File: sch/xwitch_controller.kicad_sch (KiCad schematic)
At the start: 5 parts

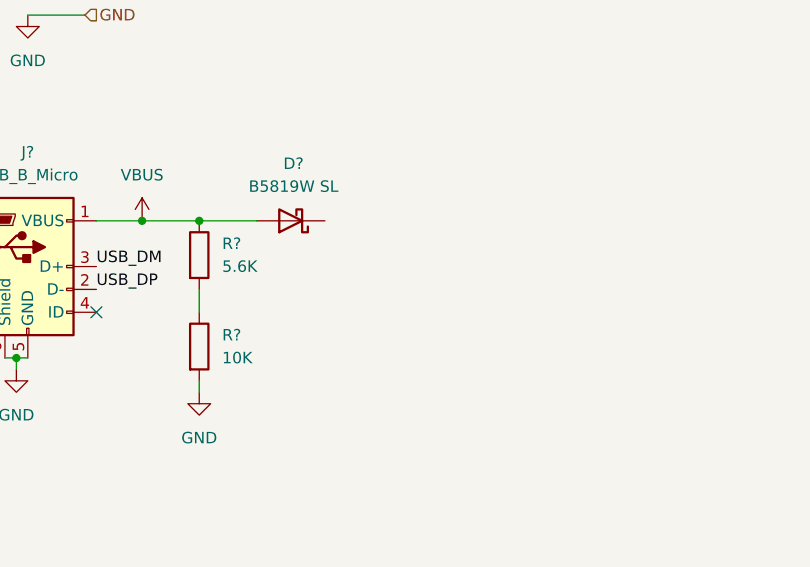
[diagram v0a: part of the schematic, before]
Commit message: added dc dc step down for rpi2040
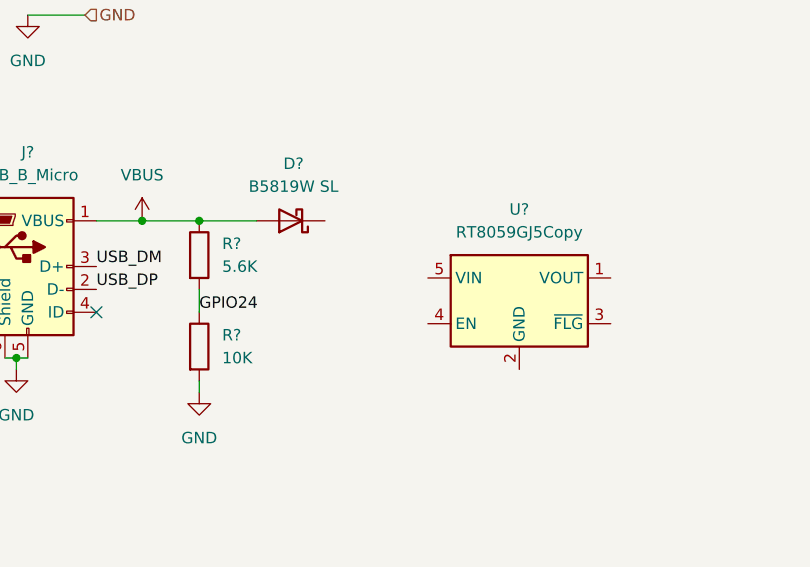
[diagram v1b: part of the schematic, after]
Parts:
- added U?: RT8059GJ5Copy, Package_TO_SOT_SMD:TSOT-23-5, symbol Power_Management:RT9742AGJ5F
- D?: LCSC C8598Copy -> C8598
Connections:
- net GPIO24: now reaches R?.1, R?.2
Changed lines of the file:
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@@
+    (effects (font (size 1.27 1.27)) (justify left bottom))
+  )
+  (label "GPIO24" (at 43.18 58.42 0)
     (effects (font (size 1.27 1.27)) (justify left bottom))
   )
@@
     )
     (pin "1")
+  )
+  (symbol (lib_id "Power_Management:RT9742AGJ5F") (at 78.74 57.15 0) (unit 1)
+    (in_bom yes) (on_board yes) (fields_autoplaced)
+    (property "Reference" "U?" (id 0) (at 78.74 46.99 0))
+    (property "Value" "RT8059GJ5Copy" (id 1) (at 78.74 49.53 0))
+    (property "Footprint" "Package_TO_SOT_SMD:TSOT-23-5" (id 2) (at 78.74 69.85 0)
+      (effects (font (size 1.27 1.27)) hide)
+    )
+    (property "Datasheet" "https://datasheet.lcsc.com/lcsc/1811100910_Richtek-Tech-RT8059GJ5_C20542.pdf" (id 3) (at 78.74 72.39 0)
+      (effects (font (size 1.27 1.27)) hide)
+    )
+    (property "LCSC" "C20542" (id 4) (at 78.74 57.15 0)
+      (effects (font (size 1.27 1.27)) hide)
+    )
+    (pin "1")
+    (pin "2")
+    (pin "3")
+    (pin "4")
+    (pin "5")
   )
   (symbol (lib_id "Connector:USB_B_Micro") (at 24.13 53.34 0) (unit 1)
@@
       (effects (font (size 1.27 1.27)) hide)
     )
-    (property "LCSC" "C8598Copy" (id 4) (at 53.34 48.26 0)
+    (property "LCSC" "C8598" (id 4) (at 53.34 48.26 0)
       (effects (font (size 1.27 1.27)) hide)
     )

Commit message: update pico schematics
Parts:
- removed U?: RT8059GJ5Copy, Package_TO_SOT_SMD:TSOT-23-5, symbol Power_Management:RT9742AGJ5F
- added C? (x2): 47u, Capacitor_SMD:C_0805_2012Metric_Pad1.18x1.45mm_HandSolder, symbol Device:C
- added C?: 2.2u, Inductor_SMD:L_0402_1005Metric_Pad0.77x0.64mm_HandSolder, symbol Device:C
- added C?: 100n, Inductor_SMD:L_0402_1005Metric_Pad0.77x0.64mm_HandSolder, symbol Device:C
- added L?: 2u2, Inductor_SMD:L_0603_1608Metric_Pad1.05x0.95mm_HandSolder, symbol Device:L
- added R?: 604K, Inductor_SMD:L_0402_1005Metric_Pad0.77x0.64mm_HandSolder, symbol Device:R
- added R?: 137K, Inductor_SMD:L_0402_1005Metric_Pad0.77x0.64mm_HandSolder, symbol Device:R
- added R? (x2): 1K, Inductor_SMD:L_0402_1005Metric_Pad0.77x0.64mm_HandSolder, symbol Device:R
- added SW?: C2689642, usb_xwitch:SW_SPST_CK_PTS636_SP43_SMTR, symbol Switch:SW_SPST
- added U?: W25Q16JVSSIQ, Package_SO:SOIC-8_5.23x5.23mm_P1.27mm, symbol Memory_Flash:W25Q32JVSS
- added U?: RT8059, Package_TO_SOT_SMD:TSOT-23-5, symbol usb_xwitch:RT8059
- added Y?: Crystal_GND24, symbol Device:Crystal_GND24
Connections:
- net +3V3: now also C?.1, C?.1, C?.1, L?.2, R?.1, U?.8 (VCC)
- net GND: now also C?.2, C?.2, C?.2, C?.2, R?.2, SW?.1 (A), U?.2 (GND), U?.4 (GND)
- net at D?.1 (K): now also C?.1, U?.1 (EN), U?.4 (VIN)
- new net: R?.1, R?.2, U?.5 (FB)
- new net: L?.1, U?.3 (LX)
- new net: R?.2, SW?.2 (B)
- new net QSPI_SCLK: U?.6 (CLK)
- new net QSPI_SD0: U?.5 (DI(IO0))
- new net QSPI_SD1: U?.2 (DO(IO1))
- new net QSPI_SD2: U?.3 (IO2)
- new net QSPI_SD3: U?.7 (IO3)
- new net QSPI_SS: R?.1, U?.1 (~{CS})
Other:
- moved on the sheet: D?, J?, R?

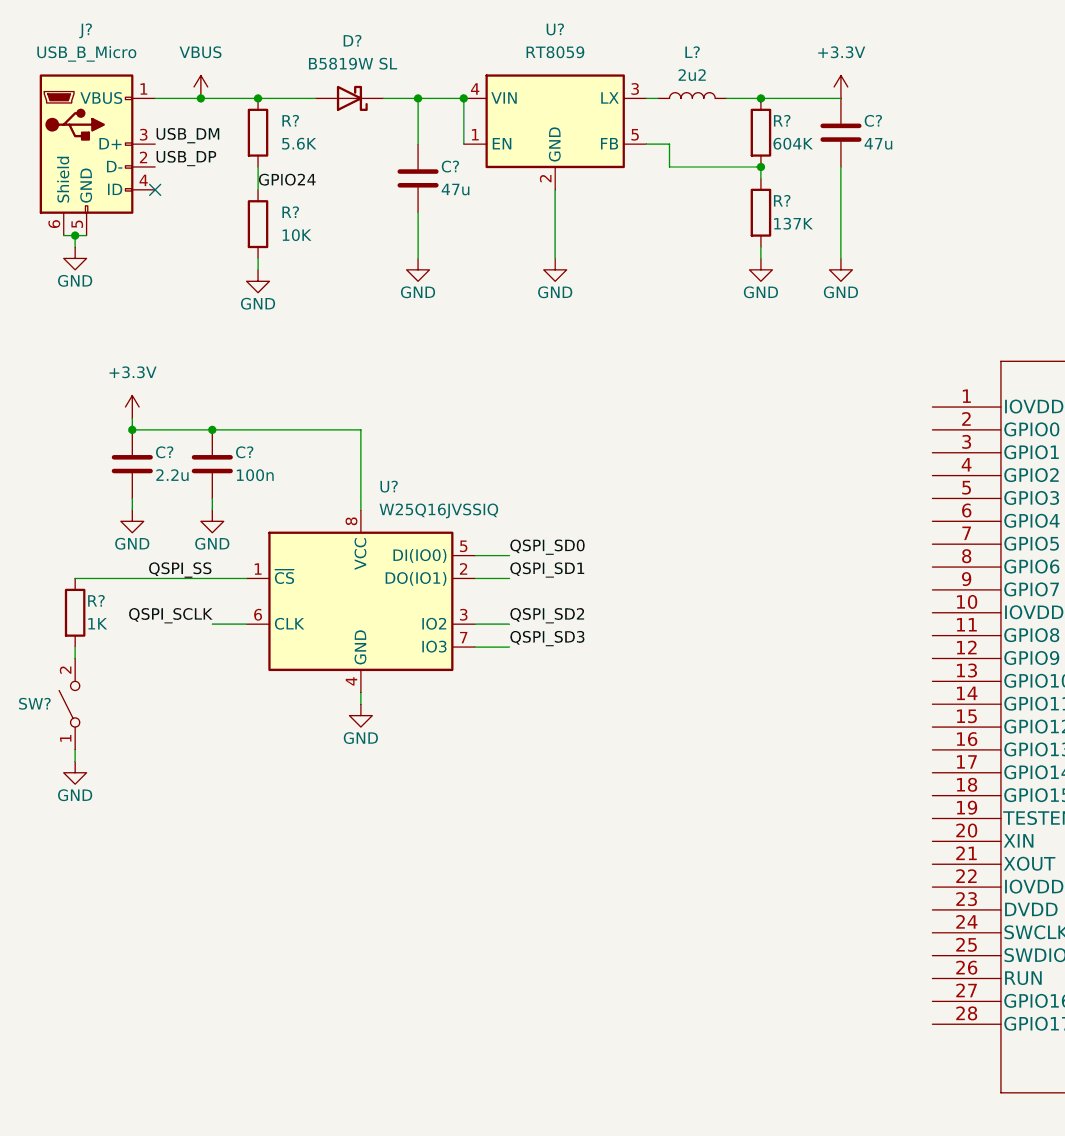
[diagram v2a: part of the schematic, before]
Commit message: update according to pico minimal design
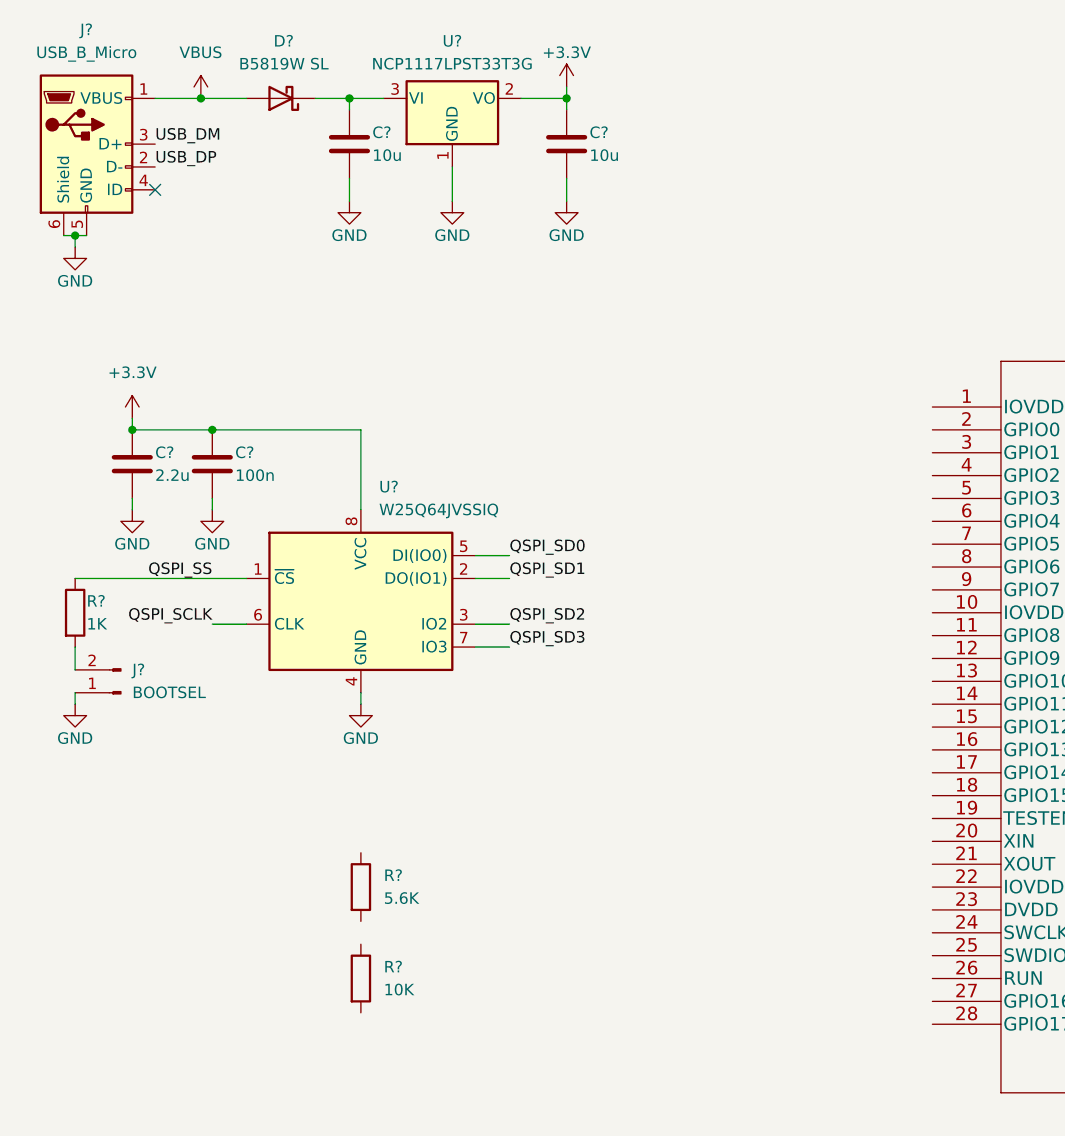
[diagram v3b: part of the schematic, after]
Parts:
- removed C?: 47u, Capacitor_SMD:C_0805_2012Metric_Pad1.18x1.45mm_HandSolder, symbol Device:C
- removed L?: 2u2, Inductor_SMD:L_0603_1608Metric_Pad1.05x0.95mm_HandSolder, symbol Device:L
- removed R?: 10K, Resistor_SMD:R_0402_1005Metric_Pad0.72x0.64mm_HandSolder, symbol Device:R
- removed R?: 604K, Inductor_SMD:L_0402_1005Metric_Pad0.77x0.64mm_HandSolder, symbol Device:R
- removed R?: 137K, Inductor_SMD:L_0402_1005Metric_Pad0.77x0.64mm_HandSolder, symbol Device:R
- removed R?: 5.6K, Resistor_SMD:R_0402_1005Metric_Pad0.72x0.64mm_HandSolder, symbol Device:R
- removed SW?: C2689642, usb_xwitch:SW_SPST_CK_PTS636_SP43_SMTR, symbol Switch:SW_SPST
- removed U?: RT8059, Package_TO_SOT_SMD:TSOT-23-5, symbol usb_xwitch:RT8059
- added C?: 10u, Capacitor_SMD:C_0603_1608Metric_Pad1.08x0.95mm_HandSolder, symbol Device:C
- added J?: BOOTSEL, Connector_PinHeader_2.54mm:PinHeader_1x02_P2.54mm_Vertical, symbol Connector:Conn_01x02_Male
- added R?: 10K, Resistor_SMD:R_0402_1005Metric_Pad0.72x0.64mm_HandSolder, symbol Device:R
- added R?: 5.6K, Resistor_SMD:R_0402_1005Metric_Pad0.72x0.64mm_HandSolder, symbol Device:R
- added U?: NCP1117LPST33T3G, Package_TO_SOT_SMD:SOT-223-3_TabPin2, symbol Regulator_Linear:NCP1117-3.3_SOT223
- C?: value 47u -> 10u; footprint Capacitor_SMD:C_0805_2012Metric_Pad1.18x1.45mm_HandSolder -> Capacitor_SMD:C_0603_1608Metric_Pad1.08x0.95mm_HandSolder; LCSC C16780 -> C96446
- J?: LCSC (none) -> C10418
- U?: value W25Q16JVSSIQ -> W25Q64JVSSIQ; LCSC C131025 -> C83140
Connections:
- net +3V3: now also C?.1, U?.2 (VO)
- net GND: now also C?.2, J?.1 (Pin_1), U?.1 (GND)
- net at C?.1, D?.1 (K): now also U?.3 (VI)
- net at R?.2: now also J?.2 (Pin_2)
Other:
- moved on the sheet: C?, D?

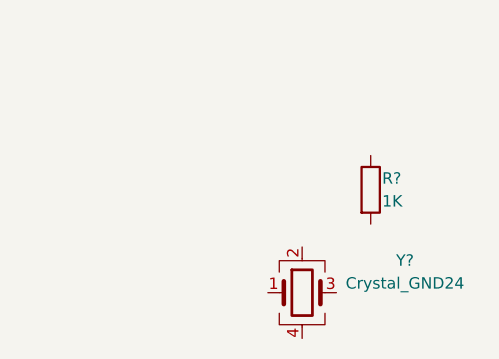
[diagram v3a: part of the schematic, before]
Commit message: update crystal symbol/foorprint
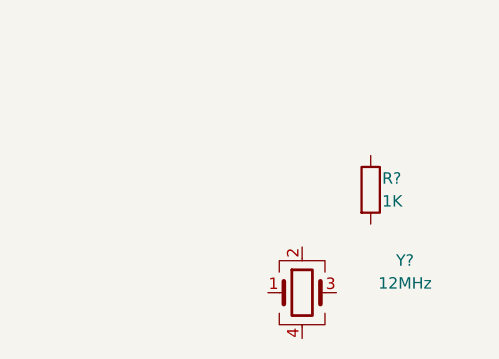
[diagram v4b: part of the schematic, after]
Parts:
- Y?: value Crystal_GND24 -> 12MHz; footprint (none) -> Crystal:Crystal_SMD_3225-4Pin_3.2x2.5mm_HandSoldering; LCSC (none) -> C9002
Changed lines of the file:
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@@
     (in_bom yes) (on_board yes) (fields_autoplaced)
     (property "Reference" "Y?" (id 0) (at 233.68 129.7686 0))
-    (property "Value" "Crystal_GND24" (id 1) (at 233.68 132.3086 0))
-    (property "Footprint" "" (id 2) (at 222.25 133.35 0)
+    (property "Value" "12MHz" (id 1) (at 233.68 132.3086 0))
+    (property "Footprint" "Crystal:Crystal_SMD_3225-4Pin_3.2x2.5mm_HandSoldering" (id 2) (at 222.25 133.35 0)
       (effects (font (size 1.27 1.27)) hide)
     )
@@
       (effects (font (size 1.27 1.27)) hide)
     )
+    (property "LCSC" "C9002" (id 4) (at 222.25 133.35 0)
+      (effects (font (size 1.27 1.27)) hide)
+    )

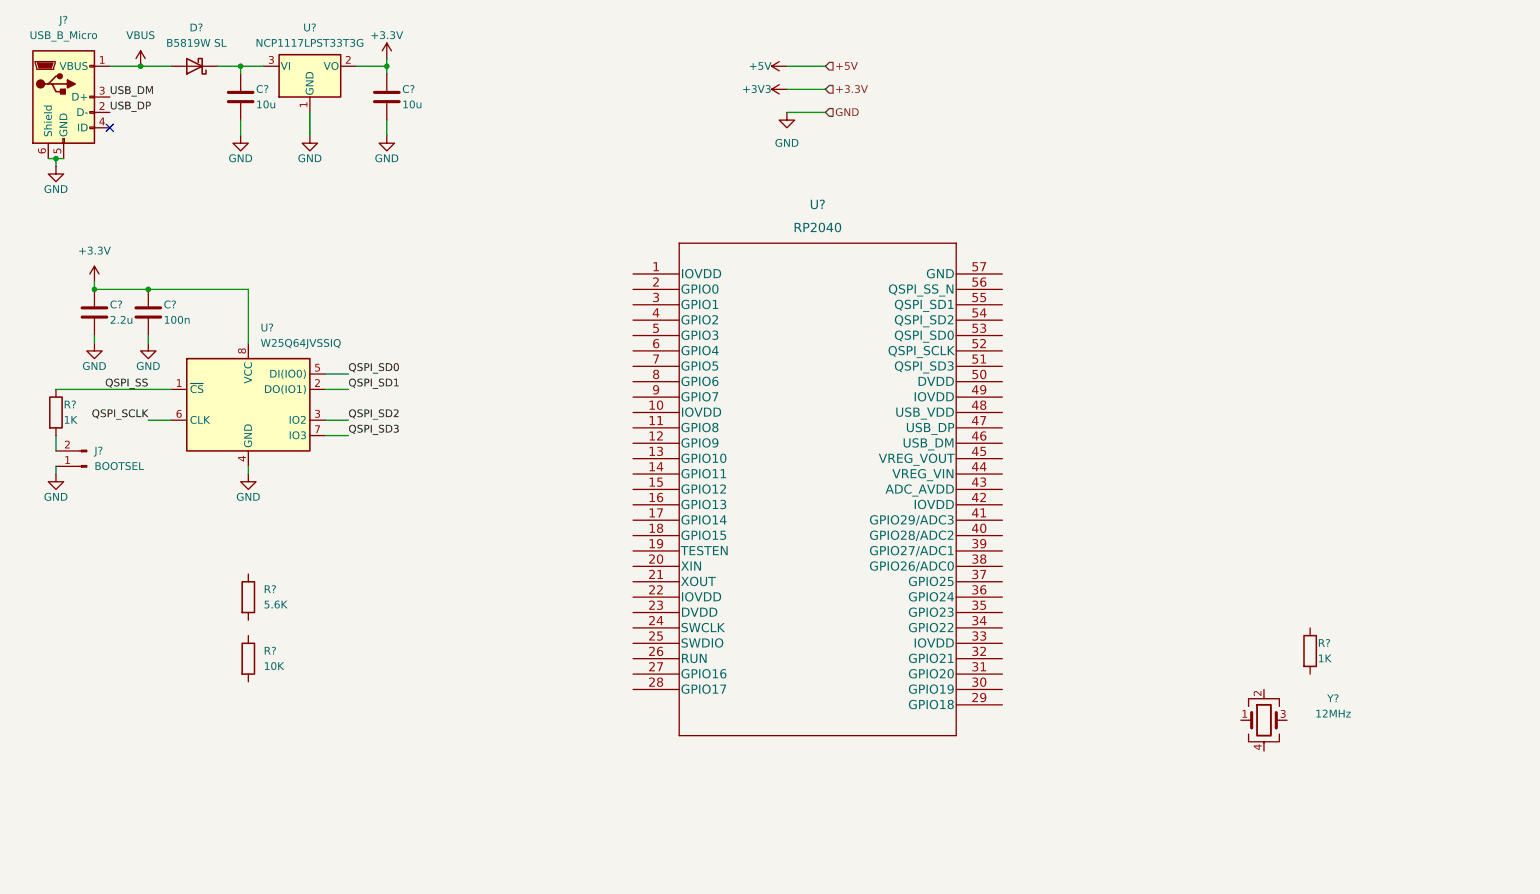
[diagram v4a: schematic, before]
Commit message: changed rp2040 to official kicad symbol and footprint
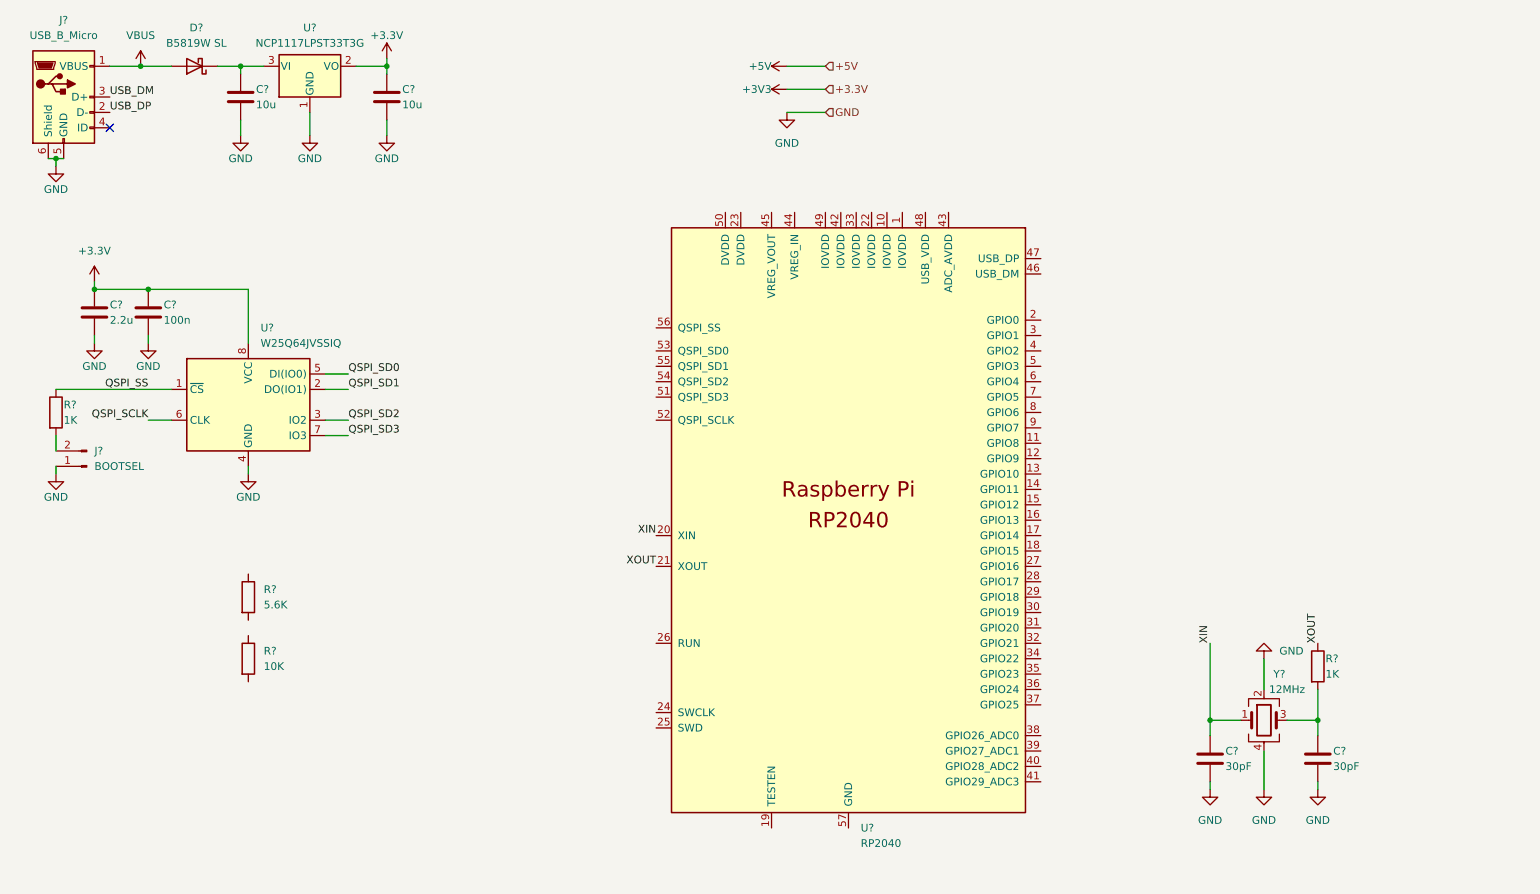
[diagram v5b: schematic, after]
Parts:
- removed U?: RP2040, usb_xwitch:RP2040, symbol usb_xwitch:RP2040
- added C? (x2): 30pF, Capacitor_SMD:C_0603_1608Metric_Pad1.08x0.95mm_HandSolder, symbol Device:C
- added U?: RP2040, usb_xwitch:RP2040-QFN-56, symbol usb_xwitch:RP2040
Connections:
- net GND: now also Y?.2, Y?.4, C?.2, C?.2
- net XIN: now reaches Y?.1
- net XIN: now also C?.1, U?.20 (XIN)
- net at Y?.3: now also R?.2, C?.1
- net XOUT: now reaches R?.1
- net XOUT: now also U?.21 (XOUT)
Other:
- moved on the sheet: R?

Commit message: updated rp2040 sch
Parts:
- removed R?: 10K, Resistor_SMD:R_0402_1005Metric_Pad0.72x0.64mm_HandSolder, symbol Device:R
- removed R?: 5.6K, Resistor_SMD:R_0402_1005Metric_Pad0.72x0.64mm_HandSolder, symbol Device:R
- added C? (x9): 100n, Resistor_SMD:R_0402_1005Metric_Pad0.72x0.64mm_HandSolder, symbol Device:C
- added C? (x2): 1u, Resistor_SMD:R_0402_1005Metric_Pad0.72x0.64mm_HandSolder, symbol Device:C
- added R? (x2): 27.4R, Resistor_SMD:R_0402_1005Metric_Pad0.72x0.64mm_HandSolder, symbol Device:R
- U?: LCSC (none) -> C2040
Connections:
- net +3V3: now also U?.1 (IOVDD), U?.10 (IOVDD), U?.22 (IOVDD), U?.33 (IOVDD), U?.42 (IOVDD), U?.43 (ADC_AVDD), U?.44 (VREG_IN), U?.48 (USB_VDD), U?.49 (IOVDD), C?.1, C?.1, C?.1, C?.1, C?.1, C?.1, C?.1, C?.1
- net +5V: now also C?.1, D?.1 (K), U?.3 (VI)
- net GND: now also U?.19 (TESTEN), U?.57 (GND), C?.2, C?.2, C?.2, C?.2, C?.2, C?.2, C?.2, C?.2, C?.2, C?.2, C?.2
- net QSPI_SCLK: now also U?.52 (QSPI_SCLK)
- net QSPI_SD0: now also U?.53 (QSPI_SD0)
- net QSPI_SD1: now also U?.55 (QSPI_SD1)
- net QSPI_SD2: now also U?.54 (QSPI_SD2)
- net QSPI_SD3: now also U?.51 (QSPI_SD3)
- net QSPI_SS: now also U?.56 (QSPI_SS)
- net +1V1: now reaches U?.23 (DVDD)
- net +1V1: now also U?.45 (VREG_VOUT), U?.50 (DVDD), C?.1, C?.1, C?.1
- net at U?.46 (USB_DM): now also R?.1
- net at U?.47 (USB_DP): now also R?.1
- net USB_DM renamed USB_D+
- net USB_D+: now also R?.2
- net USB_DP renamed USB_D-
- net USB_D-: now also R?.2
- net VBUS: no longer names the net of D?.2 (A), J?.1 (VBUS)
